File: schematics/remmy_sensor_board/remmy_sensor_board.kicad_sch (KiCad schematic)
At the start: 21 parts, among them J2 Conn_02x05_Counter_Clockwise, J3 USB_C_Receptacle_USB2.0_14P, U1 AP2112K-3.3TRG1, U2 USBLC6-2SC6, U3 TPS73219DBVT, U5 PMW3360DM-T2QU

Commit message: added images
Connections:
- net +3.3V: now also U3.3 (EN)
- net +5V: now also U1.3 (EN)
- no-connect marks 4 -> 2
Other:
- title: (none) -> Remmy B
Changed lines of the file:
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@@
 	(generator_version "8.0")
 	(paper "A4")
+	(title_block
+		(title "Remmy B")
+		(date "2025-05-18")
+		(rev "2.1")
+	)
+	(junction
+		(at 135.89 133.35)
+		(diameter 0)
+		(color 0 0 0 0)
+	)
 	(junction
 		(at 69.85 109.22)
@@
 	)
 	(junction
+		(at 72.39 161.29)
+		(diameter 0)
+		(color 0 0 0 0)
+	)
+	(junction
 		(at 69.85 88.9)
 		(diameter 0)
@@
 	)
 	(no_connect
-		(at 73.66 166.37)
-	)
-	(no_connect
 		(at 171.45 134.62)
 	)
 	(no_connect
-		(at 171.45 137.16)
-	)
-	(no_connect
 		(at 176.53 104.14)
 	)
@@
 	(wire
 		(pts
+			(xy 135.89 133.35) (xy 138.43 133.35)
+		)
+		(stroke
+			(width 0)
+			(type default)
+		)
+	)
+	(wire
+		(pts
 			(xy 53.34 129.54) (xy 53.34 132.08)
 		)
@@
 	(wire
 		(pts
+			(xy 135.89 147.32) (xy 135.89 133.35)
+		)
+		(stroke
+			(width 0)
+			(type default)
+		)
+	)
+	(wire
+		(pts
 			(xy 68.58 104.14) (xy 69.85 104.14)
 		)
@@
 	(wire
 		(pts
+			(xy 132.08 135.89) (xy 138.43 135.89)
+		)
+		(stroke
+			(width 0)
+			(type default)
+		)
+	)
+	(wire
+		(pts
 			(xy 130.81 91.44) (xy 130.81 93.98)
 		)
@@
 	(wire
 		(pts
+			(xy 171.45 137.16) (xy 171.45 147.32)
+		)
+		(stroke
+			(width 0)
+			(type default)
+		)
+	)
+	(wire
+		(pts
 			(xy 190.5 59.69) (xy 190.5 81.28)
 		)
@@
 	(wire
 		(pts
+			(xy 73.66 166.37) (xy 72.39 166.37)
+		)
+		(stroke
+			(width 0)
+			(type default)
+		)
+	)
+	(wire
+		(pts
 			(xy 115.57 101.6) (xy 113.03 101.6)
 		)
@@
 	(wire
 		(pts
-			(xy 138.43 130.81) (xy 138.43 133.35)
+			(xy 135.89 129.54) (xy 135.89 133.35)
 		)
 		(stroke
@@
 	(wire
 		(pts
+			(xy 171.45 147.32) (xy 135.89 147.32)
+		)
+		(stroke
+			(width 0)
+			(type default)
+		)
+	)
+	(wire
+		(pts
 			(xy 88.9 104.14) (xy 82.55 104.14)
 		)
@@
 	(wire
 		(pts
+			(xy 72.39 166.37) (xy 72.39 161.29)
+		)
+		(stroke
+			(width 0)
+			(type default)
+		)
+	)
+	(wire
+		(pts
 			(xy 171.45 69.85) (xy 171.45 71.12)
 		)
@@
 	(wire
 		(pts
-			(xy 138.43 137.16) (xy 138.43 135.89)
+			(xy 132.08 137.16) (xy 132.08 135.89)
 		)
 		(stroke
@@
 	(symbol
 		(lib_id "power:+3.3V")
-		(at 138.43 130.81 0)
+		(at 135.89 129.54 0)
 		(unit 1)
 		(exclude_from_sim no)
@@
 		(fields_autoplaced yes)
 		(property "Reference" "#PWR02"
-			(at 138.43 134.62 0)
+			(at 135.89 133.35 0)
 			(effects
 				(font
@@
 		)
 		(property "Value" "+3.3V"
-			(at 138.43 125.73 0)
+			(at 135.89 124.46 0)
 			(effects
 				(font
@@
 		)
 		(property "Footprint" ""
-			(at 138.43 130.81 0)
+			(at 135.89 129.54 0)
 			(effects
 				(font
@@
 		)
 		(property "Datasheet" ""
-			(at 138.43 130.81 0)
+			(at 135.89 129.54 0)
 			(effects
 				(font
@@
 		)
 		(property "Description" "Power symbol creates a global label with name \"+3.3V\""
-			(at 138.43 130.81 0)
+			(at 135.89 129.54 0)
 			(effects
 				(font
@@
 	(symbol
 		(lib_id "power:GND")
-		(at 138.43 137.16 0)
+		(at 132.08 137.16 0)
 		(unit 1)
 		(exclude_from_sim no)
@@
 		(dnp no)
 		(property "Reference" "#PWR08"
-			(at 138.43 143.51 0)
+			(at 132.08 143.51 0)
 			(effects
 				(font
@@
 		)
 		(property "Value" "GND"
-			(at 138.43 142.24 0)
+			(at 132.08 142.24 0)
 			(effects
 				(font
@@
 		)
 		(property "Footprint" ""
-			(at 138.43 137.16 0)
+			(at 132.08 137.16 0)
 			(effects
 				(font
@@
 		)
 		(property "Datasheet" ""
-			(at 138.43 137.16 0)
+			(at 132.08 137.16 0)
 			(effects
 				(font
@@
 		)
 		(property "Description" "Power symbol creates a global label with name \"GND\" , ground"
-			(at 138.43 137.16 0)
+			(at 132.08 137.16 0)
 			(effects
 				(font

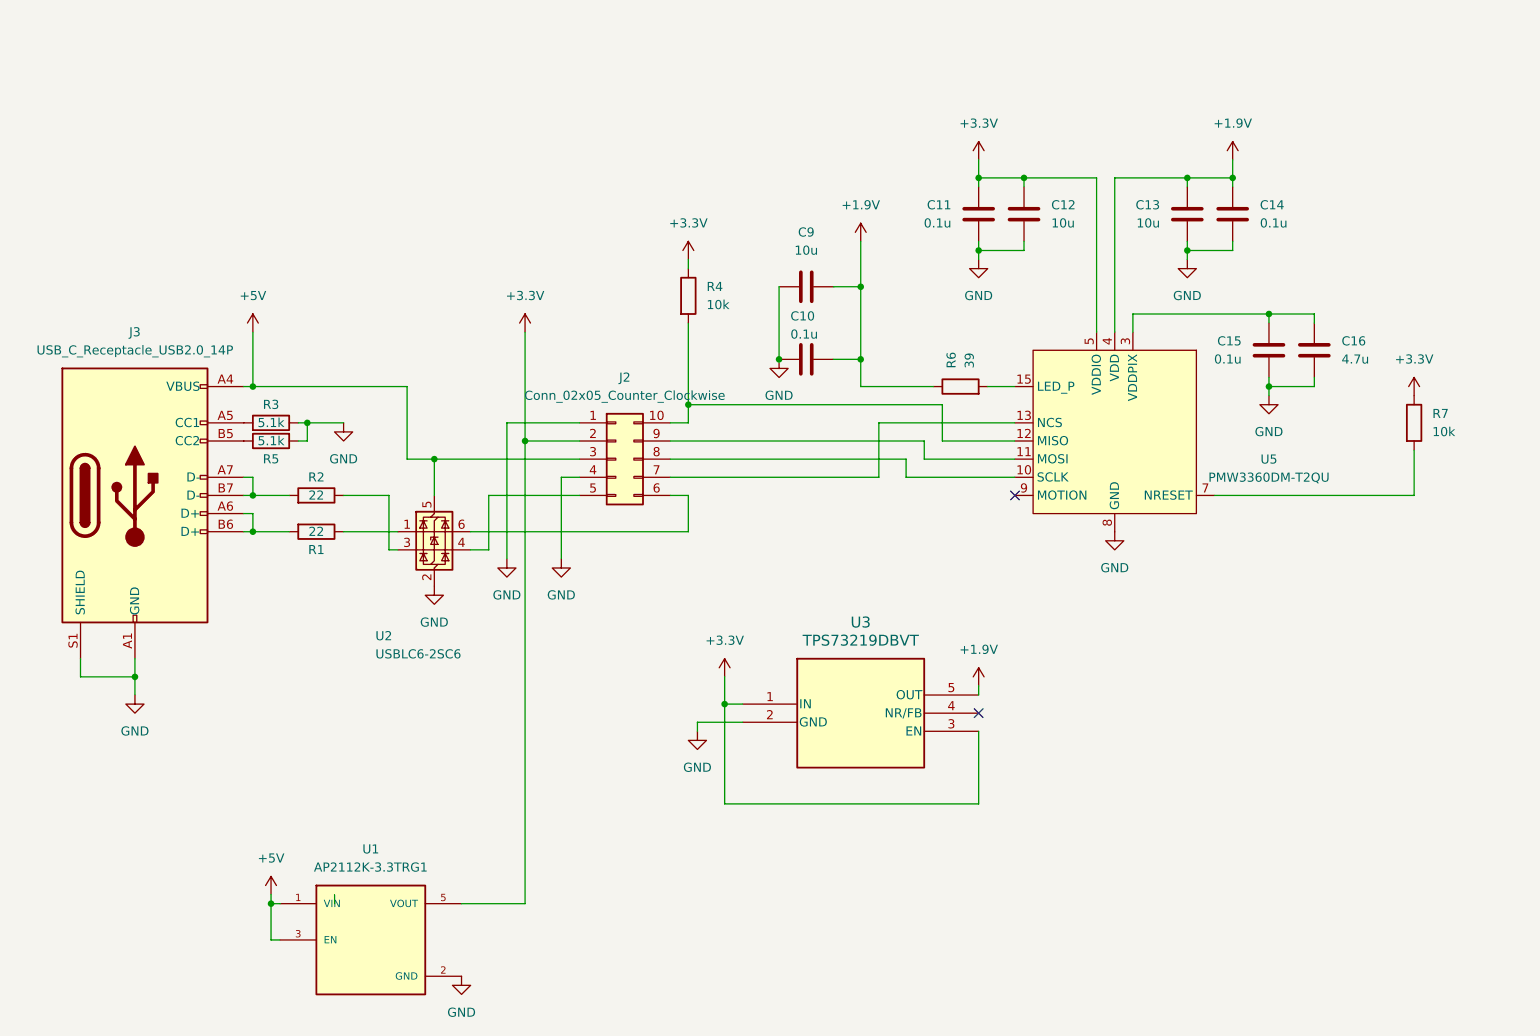
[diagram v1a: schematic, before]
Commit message: broken spi comm
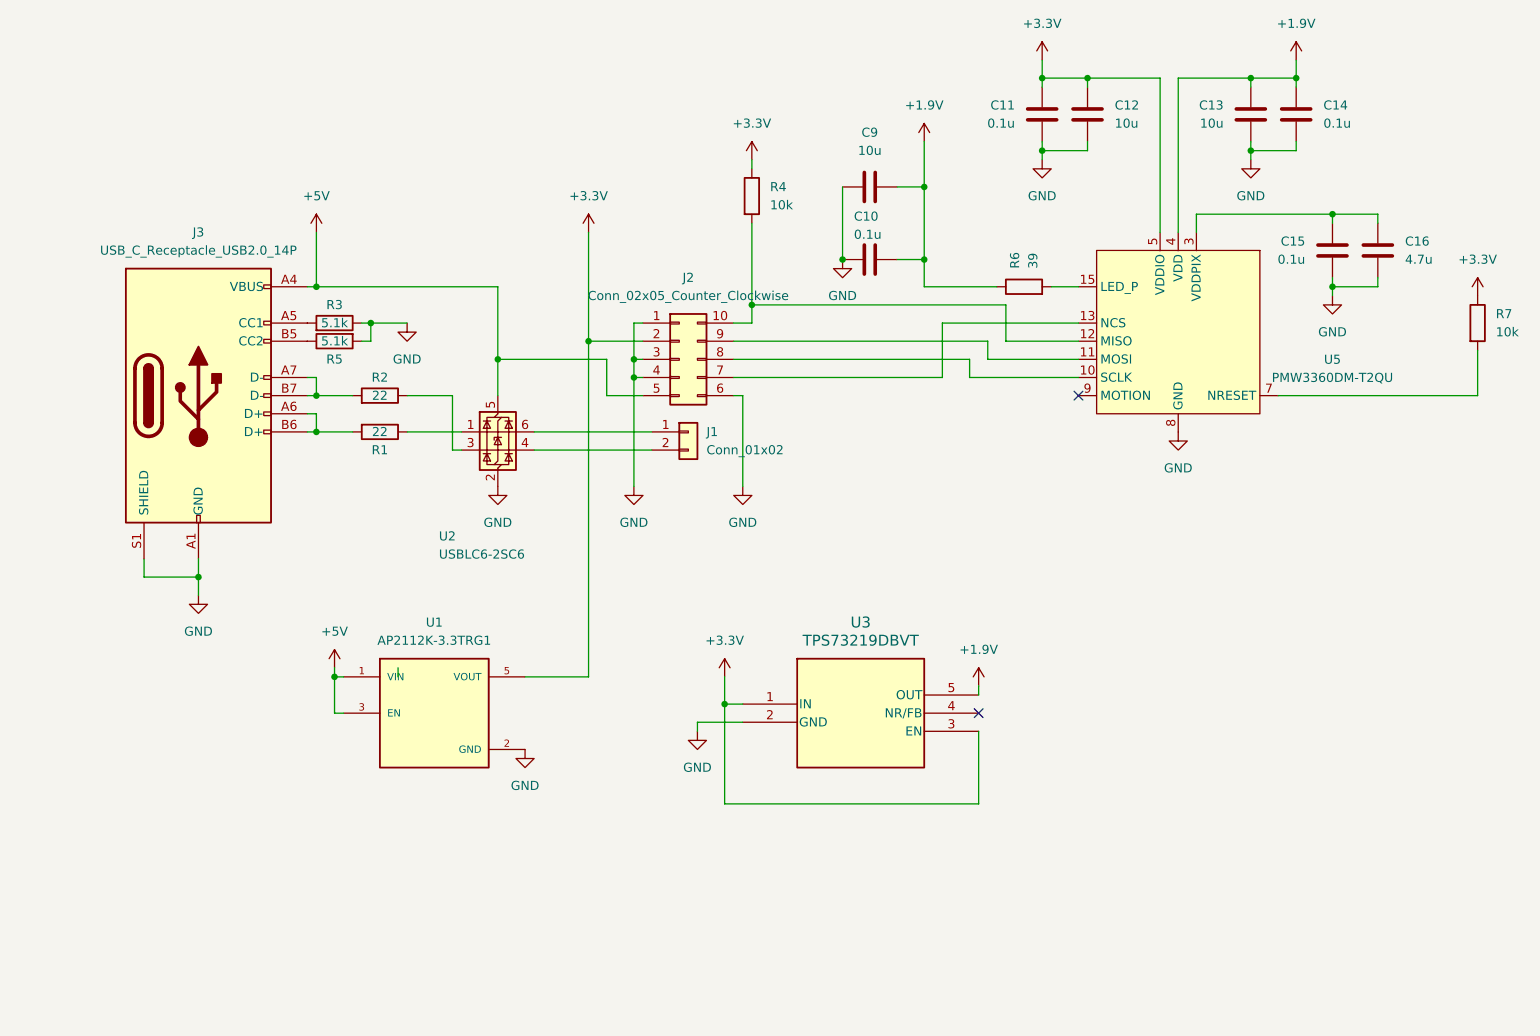
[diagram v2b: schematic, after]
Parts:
- added J1: Conn_01x02, Connector_PinSocket_1.27mm:PinSocket_1x02_P1.27mm_Vertical, symbol Connector_Generic:Conn_01x02
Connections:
- net +5V: now also J2.5 (Pin_5); no longer J2.3 (Pin_3)
- net GND: now also J2.3 (Pin_3), J2.6 (Pin_6)
- net at U2.4 (I/O2): now also J1.2 (Pin_2); no longer J2.5 (Pin_5)
- net at U2.6 (I/O1): now also J1.1 (Pin_1); no longer J2.6 (Pin_6)
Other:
- moved on the sheet: C10, C11, C12, C13, C14, C15, C16, C9, J2, J3, R1, R2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
